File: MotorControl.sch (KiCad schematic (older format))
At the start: 2 parts, among them U3 74LVC125

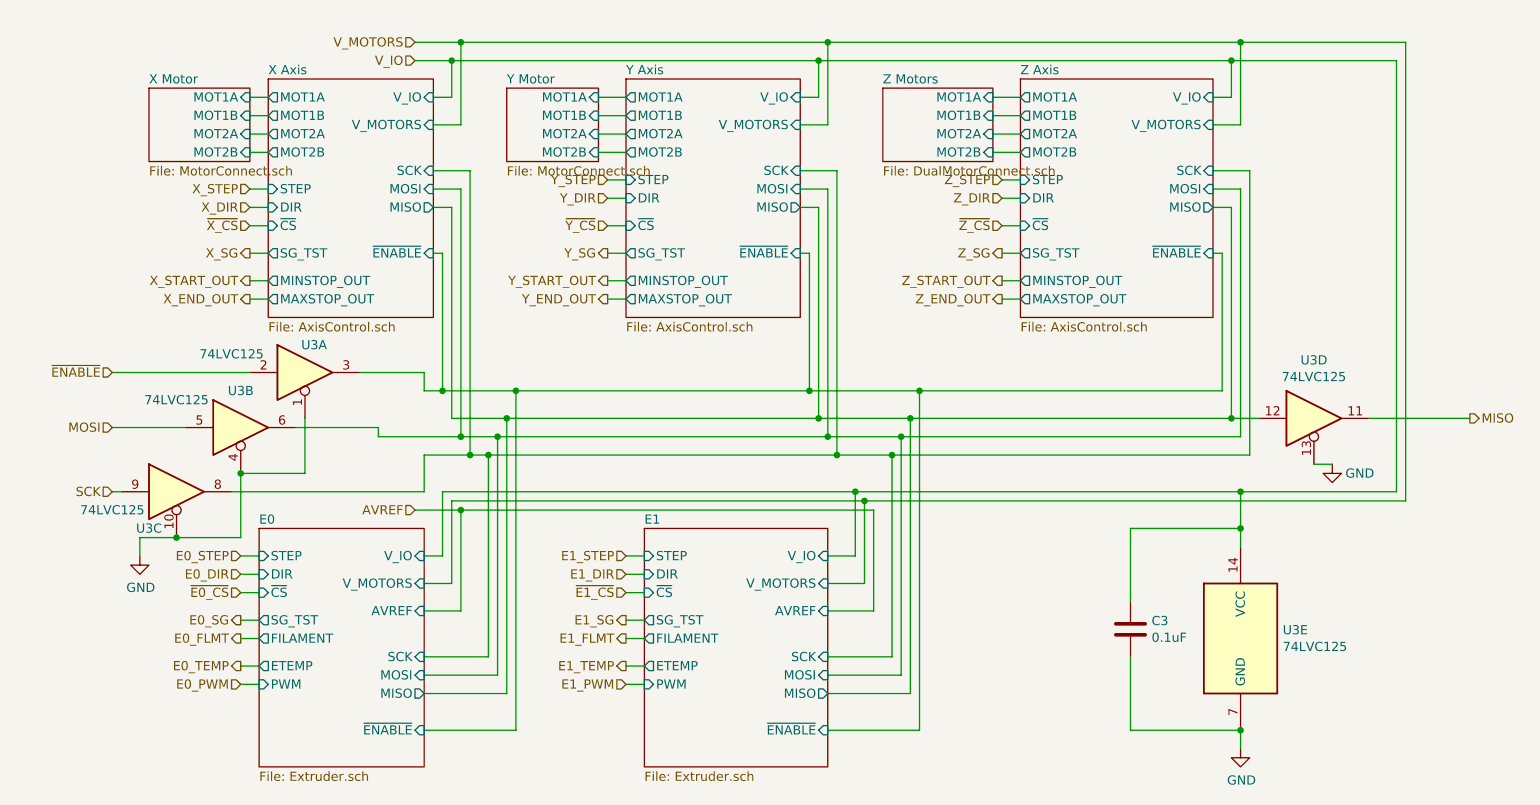
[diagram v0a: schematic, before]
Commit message: Added clock line for the motor drivers.
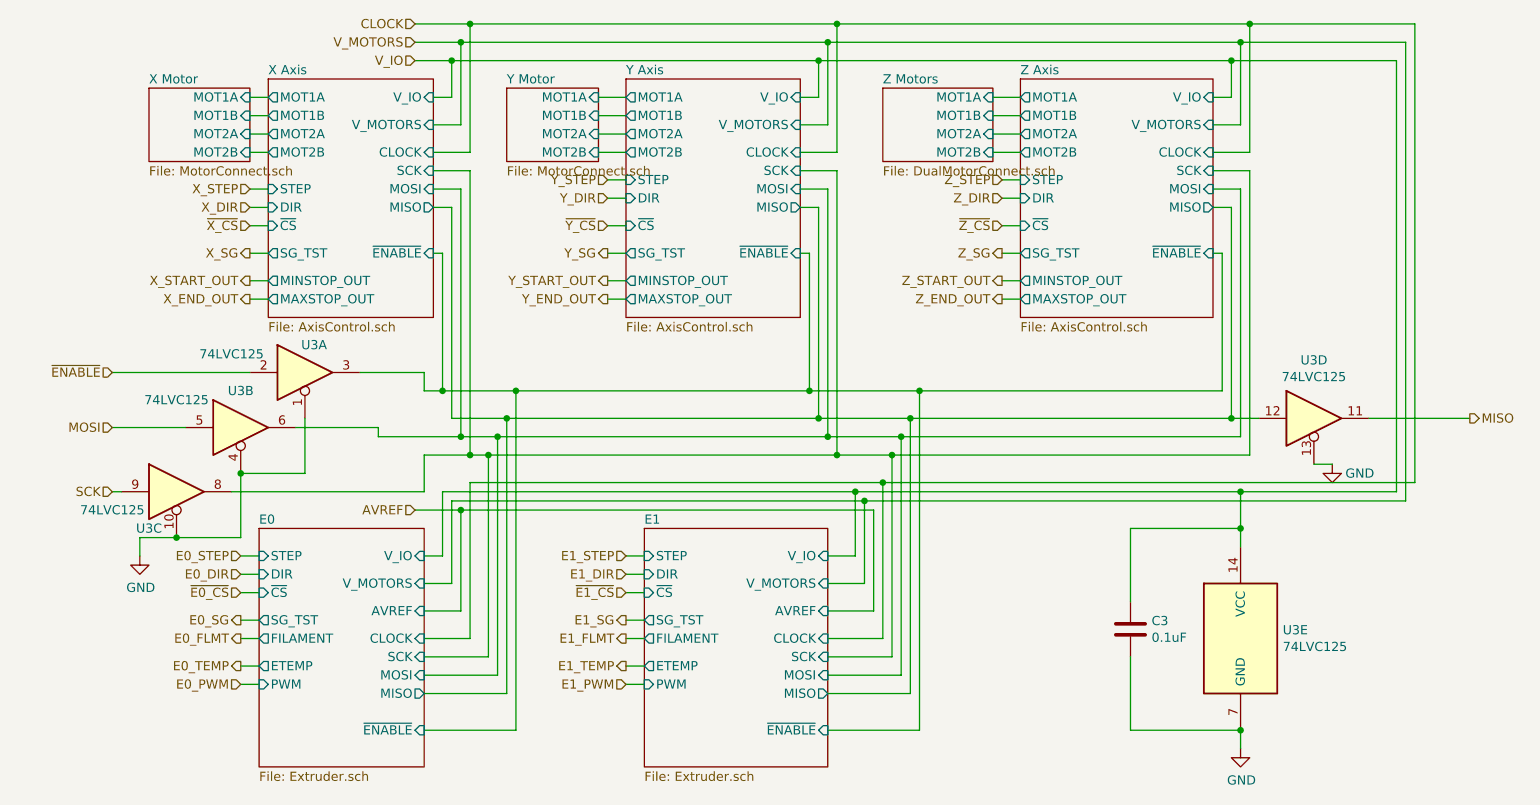
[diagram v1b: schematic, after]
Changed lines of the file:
@@
 F14 "ETEMP" O L 3350 4500 50
 F15 "PWM" I L 3350 4600 50
+F16 "CLOCK" I R 4250 4350 50
 $EndSheet
 $Sheet
@@
 F16 "MAXSTOP_OUT" O L 3400 2500 50
 F17 "MINSTOP_OUT" O L 3400 2400 50
+F18 "CLOCK" I R 4300 1700 50
 $EndSheet
 $Sheet
@@
 F16 "MAXSTOP_OUT" O L 5350 2500 50
 F17 "MINSTOP_OUT" O L 5350 2400 50
+F18 "CLOCK" I R 6300 1700 50
 $EndSheet
 Wire Wire Line
@@
 F16 "MAXSTOP_OUT" O L 7500 2500 50
 F17 "MINSTOP_OUT" O L 7500 2400 50
+F18 "CLOCK" I R 8550 1700 50
 $EndSheet
 Wire Wire Line
@@
 F14 "ETEMP" O L 5450 4500 50
 F15 "PWM" I L 5450 4600 50
+F16 "CLOCK" I R 6450 4350 50
 $EndSheet
 Wire Wire Line
@@
 	8700 4850 8700 4950
 Connection ~ 8700 4850
+Text HLabel 4200 1000 0    50   Input ~ 0
+CLOCK
+Wire Wire Line
+	4200 1000 4500 1000
+Wire Wire Line
+	4500 1000 4500 1700
+Wire Wire Line
+	4500 1700 4300 1700
+Wire Wire Line
+	4500 1000 6500 1000
+Wire Wire Line
+	6500 1000 6500 1700
+Wire Wire Line
+	6500 1700 6300 1700
+Connection ~ 4500 1000
+Wire Wire Line
+	6500 1000 8750 1000
+Wire Wire Line
+	8750 1000 8750 1700
+Wire Wire Line
+	8750 1700 8550 1700
+Connection ~ 6500 1000
+Wire Wire Line
+	4250 4350 4500 4350
+Wire Wire Line
+	4500 4350 4500 3500
+Wire Wire Line
+	4500 3500 6750 3500
+Wire Wire Line
+	6750 3500 6750 4350
+Wire Wire Line
+	6750 4350 6450 4350
+Wire Wire Line
+	6750 3500 9650 3500
+Wire Wire Line
+	9650 3500 9650 1000
+Wire Wire Line
+	9650 1000 8750 1000
+Connection ~ 6750 3500
+Connection ~ 8750 1000
 $EndSCHEMATC
